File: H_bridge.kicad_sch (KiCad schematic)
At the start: 42 parts

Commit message: Finalisations done, please produce BOM and fabricate
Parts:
- RH10, RH11, RH12, RH15, RH16, RH17, RH18, RH9: value R -> 0
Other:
- note added: "DNP"
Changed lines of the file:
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@@
     (effects (font (size 0.762 0.762)) (justify left bottom))
+  )
+  (text "DNP" (at 205.74 40.64 180)
+    (effects (font (size 1.27 1.27) bold italic) (justify right bottom))
+  )
+  (text "DNP" (at 247.65 73.66 180)
+    (effects (font (size 1.27 1.27) bold italic) (justify right bottom))
+  )
+  (text "DNP" (at 113.03 71.12 180)
+    (effects (font (size 1.27 1.27) bold italic) (justify right bottom))
+  )
+  (text "DNP" (at 104.14 86.36 180)
+    (effects (font (size 1.27 1.27) bold italic) (justify right bottom))
+  )
+  (text "DNP" (at 260.35 92.71 180)
+    (effects (font (size 1.27 1.27) bold italic) (justify right bottom))
+  )
+  (text "DNP" (at 116.84 86.36 180)
+    (effects (font (size 1.27 1.27) bold italic) (justify right bottom))
+  )
+  (text "DNP" (at 113.03 73.66 180)
+    (effects (font (size 1.27 1.27) bold italic) (justify right bottom))
   )
   (text "Bypass VINT to GND with \na 2.2uF 6.3V Capacitor" (at 130.175 133.35 0)
@@
     (effects (font (size 0.762 0.762)) (justify left bottom))
   )
+  (text "DNP" (at 114.3 76.2 180)
+    (effects (font (size 1.27 1.27) bold italic) (justify right bottom))
+  )
+  (text "DNP" (at 113.03 68.58 180)
+    (effects (font (size 1.27 1.27) bold italic) (justify right bottom))
+  )
   (text "Bypass VINT to GND with \na 2.2uF 6.3V Capacitor" (at 106.68 43.18 0)
     (effects (font (size 0.762 0.762)) (justify left bottom))
@@
   (text "10uF ceramic cap" (at 100.33 26.67 0)
     (effects (font (size 0.762 0.762)) (justify left bottom))
+  )
+  (text "DNP" (at 91.44 139.7 180)
+    (effects (font (size 1.27 1.27) bold italic) (justify right bottom))
+  )
+  (text "DNP" (at 138.43 86.36 180)
+    (effects (font (size 1.27 1.27) bold italic) (justify right bottom))
   )
   (text "There are 3 dual channel H bridges\nin this sheet,\nUse 3 channels for torquers, 3 for Magnetometer"
@@
     (effects (font (size 2.54 2.54) (thickness 0.508) bold italic) (justify left bottom))
   )
+  (text "DNP" (at 248.92 95.25 180)
+    (effects (font (size 1.27 1.27) bold italic) (justify right bottom))
+  )
+  (text "DNP" (at 247.65 71.12 180)
+    (effects (font (size 1.27 1.27) bold italic) (justify right bottom))
+  )
+  (text "DNP" (at 78.74 39.37 180)
+    (effects (font (size 1.27 1.27) bold italic) (justify right bottom))
+  )
   (text "ADDED THREE TESTPOINTS" (at 144.78 111.76 0)
     (effects (font (size 2.286 2.286) bold) (justify left bottom))
@@
   (text "0.01uF, 16V X7R ceramic cap" (at 156.845 40.64 0)
     (effects (font (size 0.762 0.762)) (justify left bottom))
+  )
+  (text "DNP" (at 127 86.36 180)
+    (effects (font (size 1.27 1.27) bold italic) (justify right bottom))
   )
   (hierarchical_label "Torquer1_2" (shape input) (at 57.15 71.12 180)
@@
     (in_bom yes) (on_board yes)
     (property "Reference" "RH12" (id 0) (at 127 169.545 90))
-    (property "Value" "R" (id 1) (at 124.46 169.545 90))
+    (property "Value" "0" (id 1) (at 124.46 169.545 90))
     (property "Footprint" "Resistor_SMD:R_0603_1608Metric" (id 2) (at 120.015 168.402 90)
       (effects (font (size 1.27 1.27)) hide)
@@
     (in_bom yes) (on_board yes)
     (property "Reference" "RH15" (id 0) (at 240.03 71.12 90))
-    (property "Value" "R" (id 1) (at 236.22 71.12 90))
+    (property "Value" "0" (id 1) (at 236.22 71.12 90))
     (property "Footprint" "Resistor_SMD:R_0603_1608Metric" (id 2) (at 232.41 69.977 90)
       (effects (font (size 1.27 1.27)) hide)
@@
     (in_bom yes) (on_board yes)
     (property "Reference" "RH11" (id 0) (at 127 167.005 90))
-    (property "Value" "R" (id 1) (at 124.46 167.005 90))
+    (property "Value" "0" (id 1) (at 124.46 167.005 90))
     (property "Footprint" "Resistor_SMD:R_0603_1608Metric" (id 2) (at 120.015 165.862 90)
       (effects (font (size 1.27 1.27)) hide)
@@
     (in_bom yes) (on_board yes)
     (property "Reference" "RH10" (id 0) (at 127 164.465 90))
-    (property "Value" "R" (id 1) (at 124.46 164.465 90))
+    (property "Value" "0" (id 1) (at 124.46 164.465 90))
     (property "Footprint" "Resistor_SMD:R_0603_1608Metric" (id 2) (at 120.015 163.322 90)
       (effects (font (size 1.27 1.27)) hide)
@@
     (in_bom yes) (on_board yes)
     (property "Reference" "RH9" (id 0) (at 127 161.925 90))
-    (property "Value" "R" (id 1) (at 124.46 161.925 90))
+    (property "Value" "0" (id 1) (at 124.46 161.925 90))
     (property "Footprint" "Resistor_SMD:R_0603_1608Metric" (id 2) (at 120.015 160.782 90)
       (effects (font (size 1.27 1.27)) hide)
@@
     (in_bom yes) (on_board yes)
     (property "Reference" "RH16" (id 0) (at 240.03 73.66 90))
-    (property "Value" "R" (id 1) (at 236.22 73.66 90))
+    (property "Value" "0" (id 1) (at 236.22 73.66 90))
     (property "Footprint" "Resistor_SMD:R_0603_1608Metric" (id 2) (at 232.41 72.517 90)
       (effects (font (size 1.27 1.27)) hide)
@@
     (in_bom yes) (on_board yes)
     (property "Reference" "RH18" (id 0) (at 240.03 78.74 90))
-    (property "Value" "R" (id 1) (at 236.22 78.74 90))
+    (property "Value" "0" (id 1) (at 236.22 78.74 90))
     (property "Footprint" "Resistor_SMD:R_0603_1608Metric" (id 2) (at 232.41 77.597 90)
       (effects (font (size 1.27 1.27)) hide)
@@
     (in_bom yes) (on_board yes)
     (property "Reference" "RH17" (id 0) (at 240.03 76.2 90))
-    (property "Value" "R" (id 1) (at 236.22 76.2 90))
+    (property "Value" "0" (id 1) (at 236.22 76.2 90))
     (property "Footprint" "Resistor_SMD:R_0603_1608Metric" (id 2) (at 232.41 75.057 90)
       (effects (font (size 1.27 1.27)) hide)

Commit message: Final Schematic
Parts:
- CH11, CH12, CH14, CH17, CH18, CH3, CH4, CH7, CH8: footprint Capacitor_SMD:C_0603_1608Metric -> Capacitor_SMD:C_0603_1608Metric_Pad1.08x0.95mm_HandSolder
- RH15, RH16, RH5, RH6, RH7, RH8: footprint Resistor_SMD:R_0603_1608Metric -> Resistor_SMD:R_0603_1608Metric_Pad0.98x0.95mm_HandSolder
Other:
- note removed: "ADDED THREE TESTPOINTS"
- note removed: "Sheet designator H"
- note removed: "There are 3 dual channel H bridges in this sheet, Use 3 channels for torquers, 3 for Magnetometer"
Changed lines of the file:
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@@
     (effects (font (size 1.27 1.27) bold italic) (justify right bottom))
-  )
-  (text "There are 3 dual channel H bridges\nin this sheet,\nUse 3 channels for torquers, 3 for Magnetometer"
-    (at 184.785 163.83 0)
-    (effects (font (size 1.905 1.905)) (justify left bottom))
   )
   (text "nsleep-\n	Low - 0.5V max\n	High - 2.5V min" (at 39.37 189.865 180)
     (effects (font (size 1.905 1.905) bold italic) (justify right bottom))
   )
-  (text "Sheet designator H \n" (at 234.95 139.7 0)
-    (effects (font (size 2.54 2.54) (thickness 0.508) bold italic) (justify left bottom))
-  )
   (text "DNP" (at 248.92 95.25 180)
     (effects (font (size 1.27 1.27) bold italic) (justify right bottom))
@@
     (effects (font (size 1.27 1.27) bold italic) (justify right bottom))
   )
-  (text "ADDED THREE TESTPOINTS" (at 144.78 111.76 0)
-    (effects (font (size 2.286 2.286) bold) (justify left bottom))
-  )
   (text "0.01uF, 16V X7R ceramic cap" (at 156.845 40.64 0)
     (effects (font (size 0.762 0.762)) (justify left bottom))
@@
       (effects (font (size 1.27 1.27)) (justify left))
     )
-    (property "Footprint" "Capacitor_SMD:C_0603_1608Metric" (id 2) (at 199.39 43.18 0)
+    (property "Footprint" "Capacitor_SMD:C_0603_1608Metric_Pad1.08x0.95mm_HandSolder" (id 2) (at 199.39 43.18 0)
       (effects (font (size 1.27 1.27)) hide)
     )
@@
     (property "Reference" "RH7" (id 0) (at 106.68 73.025 90))
     (property "Value" "R" (id 1) (at 104.775 73.025 90))
-    (property "Footprint" "Resistor_SMD:R_0603_1608Metric" (id 2) (at 100.33 75.438 90)
+    (property "Footprint" "Resistor_SMD:R_0603_1608Metric_Pad0.98x0.95mm_HandSolder" (id 2) (at 100.33 75.438 90)
       (effects (font (size 1.27 1.27)) hide)
     )
@@
       (effects (font (size 1.27 1.27)) (justify left))
     )
-    (property "Footprint" "Capacitor_SMD:C_0603_1608Metric" (id 2) (at 252.73 86.995 0)
+    (property "Footprint" "Capacitor_SMD:C_0603_1608Metric_Pad1.08x0.95mm_HandSolder" (id 2) (at 252.73 86.995 0)
       (effects (font (size 1.27 1.27)) hide)
     )
@@
     (property "Reference" "RH15" (id 0) (at 240.03 71.12 90))
     (property "Value" "0" (id 1) (at 236.22 71.12 90))
-    (property "Footprint" "Resistor_SMD:R_0603_1608Metric" (id 2) (at 232.41 69.977 90)
+    (property "Footprint" "Resistor_SMD:R_0603_1608Metric_Pad0.98x0.95mm_HandSolder" (id 2) (at 232.41 69.977 90)
       (effects (font (size 1.27 1.27)) hide)
     )
@@
     (property "Reference" "RH6" (id 0) (at 106.68 70.485 90))
     (property "Value" "R" (id 1) (at 104.775 70.485 90))
-    (property "Footprint" "Resistor_SMD:R_0603_1608Metric" (id 2) (at 100.33 72.898 90)
+    (property "Footprint" "Resistor_SMD:R_0603_1608Metric_Pad0.98x0.95mm_HandSolder" (id 2) (at 100.33 72.898 90)
       (effects (font (size 1.27 1.27)) hide)
     )
@@
       (effects (font (size 1.27 1.27)) (justify left))
     )
-    (property "Footprint" "Capacitor_SMD:C_0603_1608Metric" (id 2) (at 121.92 88.9 0)
+    (property "Footprint" "Capacitor_SMD:C_0603_1608Metric_Pad1.08x0.95mm_HandSolder" (id 2) (at 121.92 88.9 0)
       (effects (font (size 1.27 1.27)) hide)
     )
@@
       (effects (font (size 1.27 1.27)) (justify left))
     )
-    (property "Footprint" "Capacitor_SMD:C_0603_1608Metric" (id 2) (at 99.06 88.9 0)
+    (property "Footprint" "Capacitor_SMD:C_0603_1608Metric_Pad1.08x0.95mm_HandSolder" (id 2) (at 99.06 88.9 0)
       (effects (font (size 1.27 1.27)) hide)
     )
@@
       (effects (font (size 1.27 1.27)) (justify left))
     )
-    (property "Footprint" "Capacitor_SMD:C_0603_1608Metric" (id 2) (at 72.39 41.275 0)
+    (property "Footprint" "Capacitor_SMD:C_0603_1608Metric_Pad1.08x0.95mm_HandSolder" (id 2) (at 72.39 41.275 0)
       (effects (font (size 1.27 1.27)) hide)
     )
@@
       (effects (font (size 1.27 1.27)) (justify left))
     )
-    (property "Footprint" "Capacitor_SMD:C_0603_1608Metric" (id 2) (at 111.76 88.9 0)
+    (property "Footprint" "Capacitor_SMD:C_0603_1608Metric_Pad1.08x0.95mm_HandSolder" (id 2) (at 111.76 88.9 0)
       (effects (font (size 1.27 1.27)) hide)
     )
@@
     (property "Reference" "RH8" (id 0) (at 107.315 75.565 90))
     (property "Value" "R" (id 1) (at 104.775 75.565 90))
-    (property "Footprint" "Resistor_SMD:R_0603_1608Metric" (id 2) (at 100.33 74.422 90)
+    (property "Footprint" "Resistor_SMD:R_0603_1608Metric_Pad0.98x0.95mm_HandSolder" (id 2) (at 100.33 74.422 90)
       (effects (font (size 1.27 1.27)) hide)
     )
@@
     (property "Reference" "RH5" (id 0) (at 106.68 67.945 90))
     (property "Value" "R" (id 1) (at 104.775 67.945 90))
-    (property "Footprint" "Resistor_SMD:R_0603_1608Metric" (id 2) (at 100.33 70.358 90)
+    (property "Footprint" "Resistor_SMD:R_0603_1608Metric_Pad0.98x0.95mm_HandSolder" (id 2) (at 100.33 70.358 90)
       (effects (font (size 1.27 1.27)) hide)
     )
@@
       (effects (font (size 1.27 1.27)) (justify left))
     )
-    (property "Footprint" "Capacitor_SMD:C_0603_1608Metric" (id 2) (at 85.725 135.255 0)
+    (property "Footprint" "Capacitor_SMD:C_0603_1608Metric_Pad1.08x0.95mm_HandSolder" (id 2) (at 85.725 135.255 0)
       (effects (font (size 1.27 1.27)) hide)
     )
@@
     (property "Reference" "RH16" (id 0) (at 240.03 73.66 90))
     (property "Value" "0" (id 1) (at 236.22 73.66 90))
-    (property "Footprint" "Resistor_SMD:R_0603_1608Metric" (id 2) (at 232.41 72.517 90)
+    (property "Footprint" "Resistor_SMD:R_0603_1608Metric_Pad0.98x0.95mm_HandSolder" (id 2) (at 232.41 72.517 90)
       (effects (font (size 1.27 1.27)) hide)
     )
@@
       (effects (font (size 1.27 1.27)) (justify left))
     )
-    (property "Footprint" "Capacitor_SMD:C_0603_1608Metric" (id 2) (at 243.84 90.17 0)
+    (property "Footprint" "Capacitor_SMD:C_0603_1608Metric_Pad1.08x0.95mm_HandSolder" (id 2) (at 243.84 90.17 0)
       (effects (font (size 1.27 1.27)) hide)
     )
@@
       (effects (font (size 1.27 1.27)) (justify left))
     )
-    (property "Footprint" "Capacitor_SMD:C_0603_1608Metric" (id 2) (at 132.08 88.9 0)
-      (effects (font (size 1.27 1.27)) hide)
-    )
+    (property "Footprint" "Capacitor_SMD:C_0603_1608Metric_Pad1.08x0.95mm_HandSolder" (id 2) (at 132.08 88.9 0)
+      (effects (font (size 1.27 1.27)) hide)
+    )

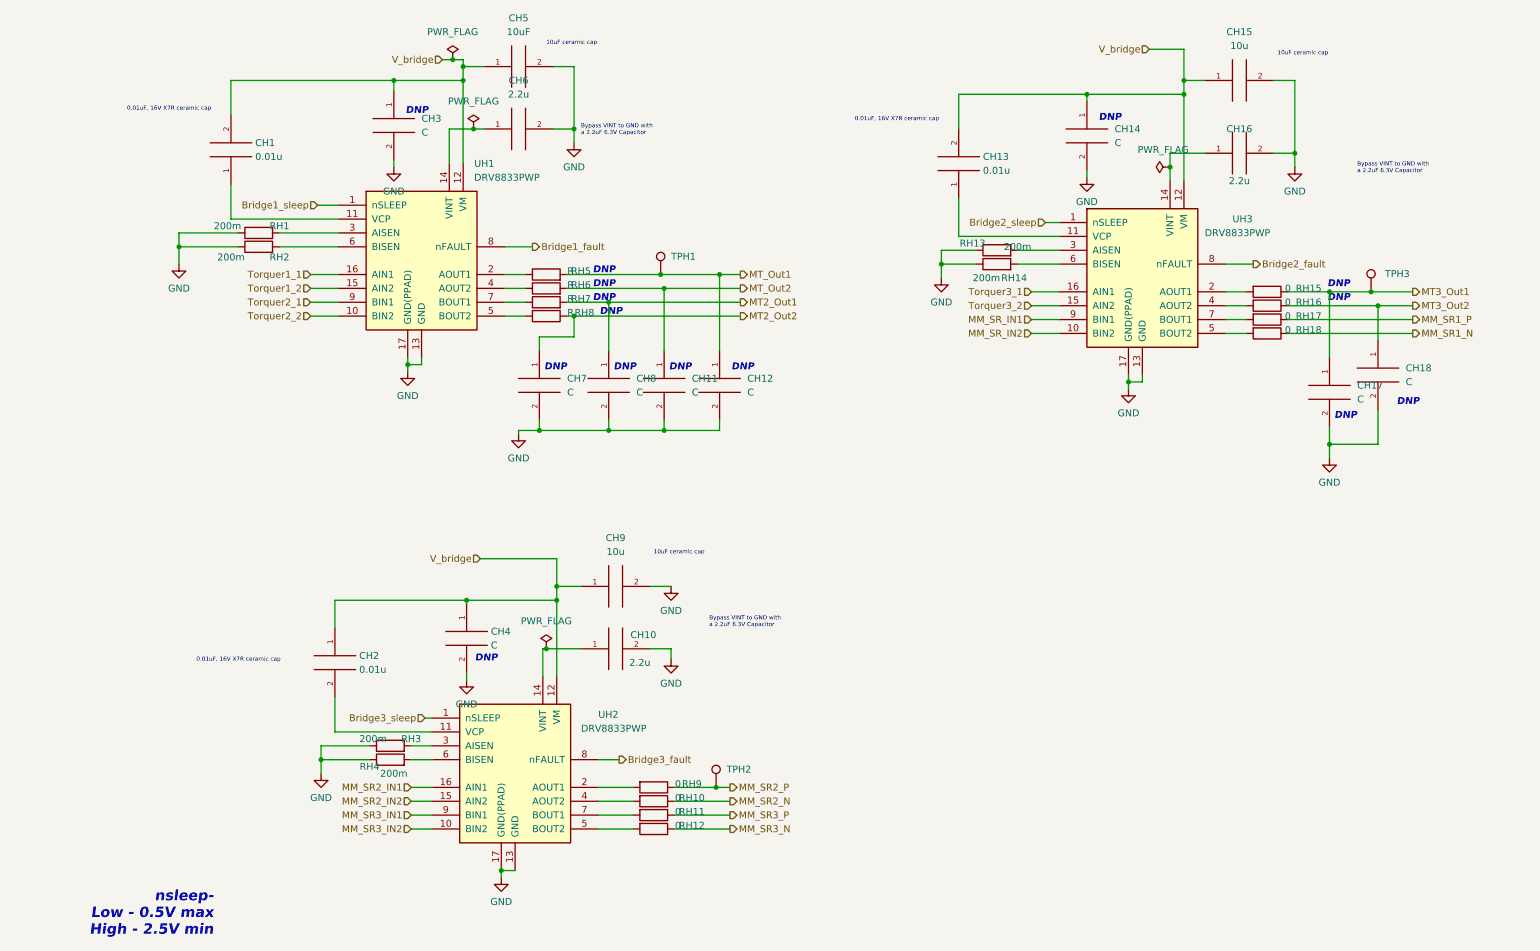
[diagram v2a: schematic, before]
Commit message: MCU circuitry forgot LOL
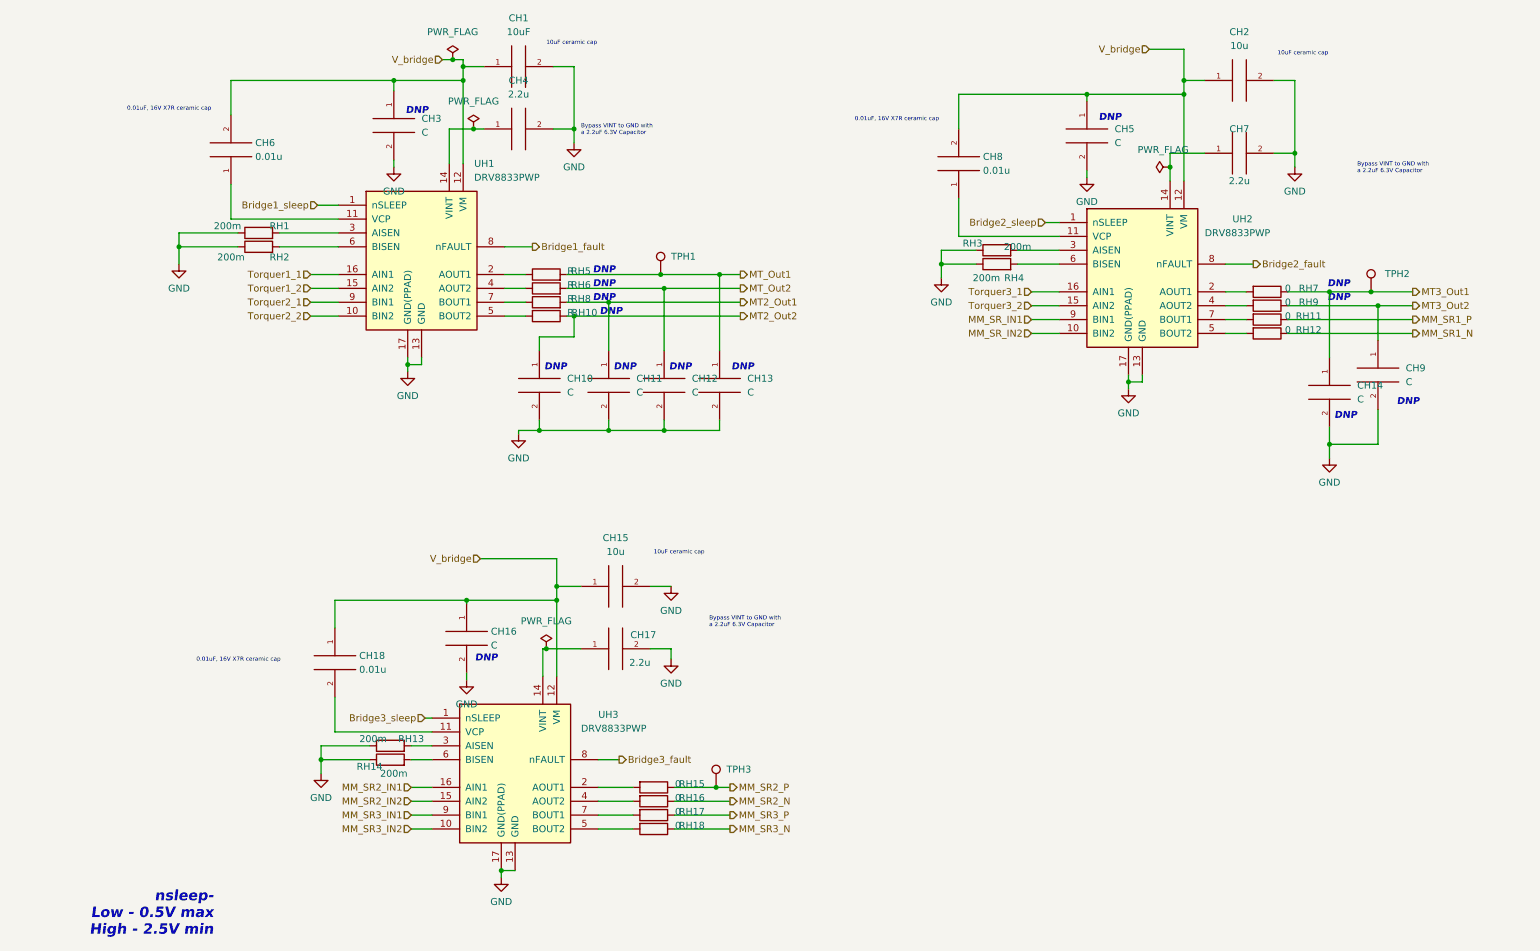
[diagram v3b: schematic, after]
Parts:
- renumbered CH5 to CH1, CH7 to CH10, CH8 to CH11, CH11 to CH12, CH12 to CH13, CH17 to CH14, CH9 to CH15, CH4 to CH16, CH10 to CH17, CH2 to CH18, CH15 to CH2, CH6 to CH4, CH14 to CH5, CH1 to CH6, CH16 to CH7, CH13 to CH8, CH18 to CH9, RH8 to RH10, RH17 to RH11, RH18 to RH12, RH3 to RH13, RH4 to RH14, RH9 to RH15, RH10 to RH16, RH11 to RH17, RH12 to RH18, RH13 to RH3, RH14 to RH4, RH15 to RH7, RH7 to RH8, RH16 to RH9, TPH3 to TPH2, TPH2 to TPH3, UH3 to UH2, UH2 to UH3
